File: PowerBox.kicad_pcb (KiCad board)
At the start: 2 copper layers, 71.1 x 76.2 mm, 7 parts, among them J1 Screw_Terminal_01x16, U1 MP1584EN, U2 MP1584EN, U3 MP1584EN, U4 MP1584EN, U5 MP1584EN, U6 MP1584EN

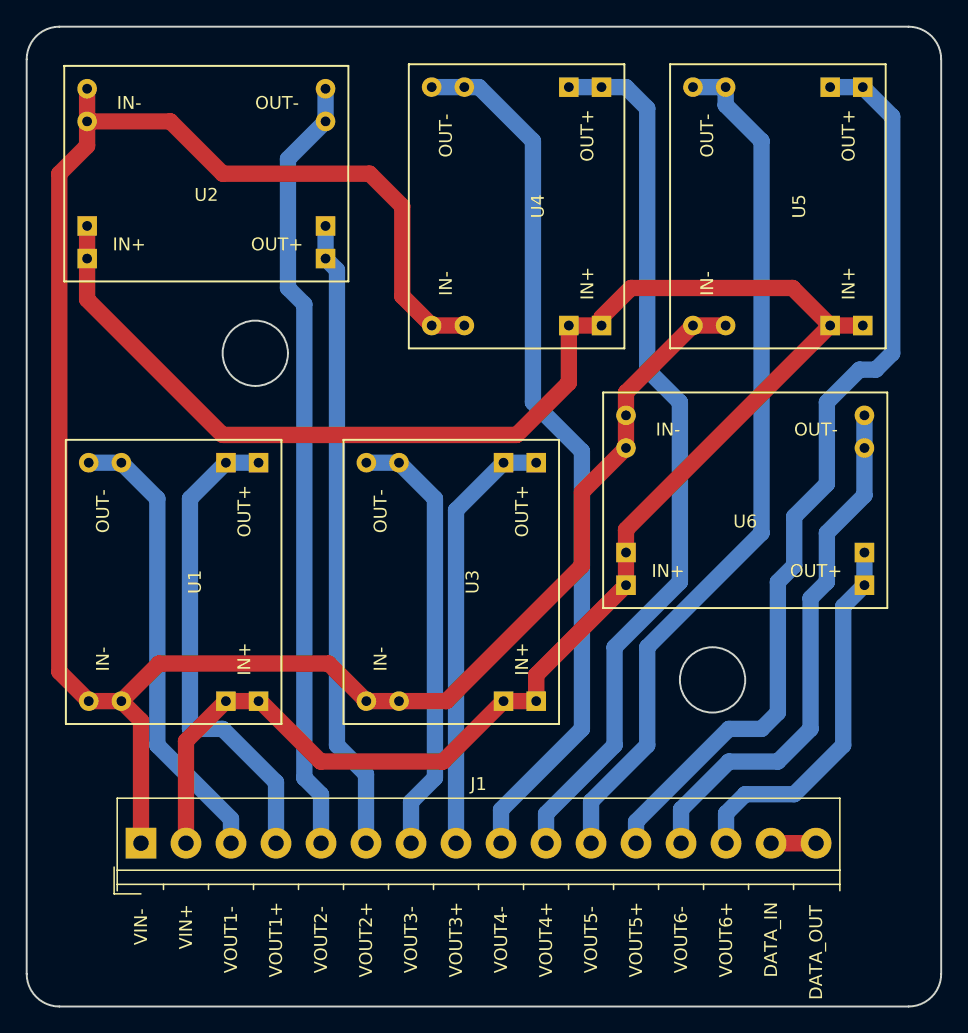
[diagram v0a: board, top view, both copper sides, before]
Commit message: rerouted some tracks away from screw holes, with 25 mil grid.
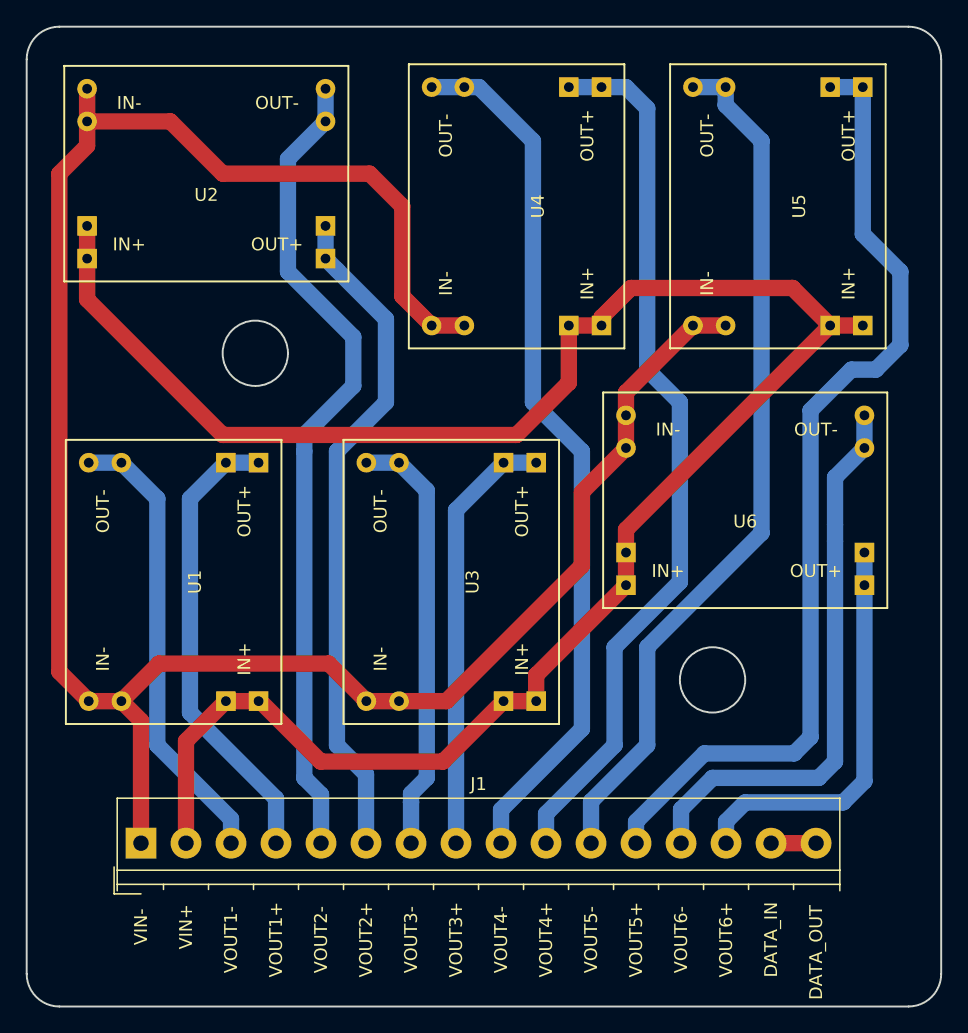
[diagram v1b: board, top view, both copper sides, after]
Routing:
- net Net-(J1-Pad12): track 72.8 -> 76.3 mm
- net Net-(J1-Pad5): track 60.9 -> 64.1 mm
- net Net-(J1-Pad6): track 49.3 -> 52.5 mm
- net Net-(J1-Pad13): track 41.4 -> 44.0 mm
- net Net-(J1-Pad14): track 29.3 -> 31.5 mm
- net Net-(J1-Pad4): track 38.0 -> 36.5 mm
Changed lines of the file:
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@@
     (thickness 1.6)
     (drawings 10)
-    (tracks 144)
+    (tracks 146)
     (zones 0)
     (modules 7)
@@
   (segment (start 111.76 106.68) (end 117.49 112.41) (width 1.27) (layer B.Cu) (net 3))
   (segment (start 117.49 112.41) (end 117.49 114.3) (width 1.27) (layer B.Cu) (net 3))
-  (segment (start 114.3 105.41) (end 116.84 105.41) (width 1.27) (layer B.Cu) (net 4))
-  (segment (start 114.3 87.503) (end 114.3 105.41) (width 1.27) (layer B.Cu) (net 4))
+  (segment (start 114.3 87.503) (end 114.3 104.14) (width 1.27) (layer B.Cu) (net 4))
   (segment (start 117.094 84.709) (end 114.3 87.503) (width 1.27) (layer B.Cu) (net 4))
-  (segment (start 120.99 109.56) (end 120.99 114.3) (width 1.27) (layer B.Cu) (net 4))
-  (segment (start 116.84 105.41) (end 120.99 109.56) (width 1.27) (layer B.Cu) (net 4))
+  (segment (start 120.99 110.83) (end 120.99 114.3) (width 1.27) (layer B.Cu) (net 4) (status 800000))
+  (segment (start 114.3 104.14) (end 120.99 110.83) (width 1.27) (layer B.Cu) (net 4))
   (segment (start 119.634 84.709) (end 117.094 84.709) (width 1.27) (layer B.Cu) (net 4))
   (segment (start 120.65 113.96) (end 120.99 114.3) (width 1.27) (layer B.Cu) (net 4))
-  (segment (start 124.841 55.626) (end 124.841 58.166) (width 1.27) (layer B.Cu) (net 5))
+  (segment (start 123.19 83.82) (end 123.19 82.55) (width 1.27) (layer B.Cu) (net 5))
   (segment (start 124.841 58.166) (end 121.92 61.087) (width 1.27) (layer B.Cu) (net 5))
-  (segment (start 121.92 61.087) (end 121.92 71.12) (width 1.27) (layer B.Cu) (net 5))
-  (segment (start 121.92 71.12) (end 123.19 72.39) (width 1.27) (layer B.Cu) (net 5))
-  (segment (start 123.19 72.39) (end 123.19 109.22) (width 1.27) (layer B.Cu) (net 5))
   (segment (start 123.19 109.22) (end 124.49 110.52) (width 1.27) (layer B.Cu) (net 5))
   (segment (start 124.49 110.52) (end 124.49 114.3) (width 1.27) (layer B.Cu) (net 5))
-  (segment (start 127.99 114.3) (end 127.99 108.94) (width 1.27) (layer B.Cu) (net 6))
-  (segment (start 125.73 69.723) (end 124.841 68.834) (width 1.27) (layer B.Cu) (net 6))
-  (segment (start 125.73 106.68) (end 125.73 69.723) (width 1.27) (layer B.Cu) (net 6))
+  (segment (start 123.19 109.22) (end 123.19 83.82) (width 1.27) (layer B.Cu) (net 5))
+  (segment (start 121.92 69.85) (end 121.92 61.087) (width 1.27) (layer B.Cu) (net 5))
+  (segment (start 127 74.93) (end 121.92 69.85) (width 1.27) (layer B.Cu) (net 5))
+  (segment (start 127 78.74) (end 127 74.93) (width 1.27) (layer B.Cu) (net 5))
+  (segment (start 123.19 82.55) (end 127 78.74) (width 1.27) (layer B.Cu) (net 5))
+  (segment (start 124.841 55.626) (end 124.841 58.166) (width 1.27) (layer B.Cu) (net 5))
+  (segment (start 125.73 106.68) (end 125.73 83.82) (width 1.27) (layer B.Cu) (net 6))
   (segment (start 127.99 108.94) (end 125.73 106.68) (width 1.27) (layer B.Cu) (net 6))
+  (segment (start 124.841 68.834) (end 125.73 69.723) (width 1.27) (layer B.Cu) (net 6))
+  (segment (start 127.99 108.94) (end 127.99 114.3) (width 1.27) (layer B.Cu) (net 6))
+  (segment (start 129.54 73.533) (end 125.73 69.723) (width 1.27) (layer B.Cu) (net 6))
+  (segment (start 129.54 80.01) (end 129.54 73.533) (width 1.27) (layer B.Cu) (net 6))
+  (segment (start 125.73 83.82) (end 129.54 80.01) (width 1.27) (layer B.Cu) (net 6))
   (segment (start 124.841 68.834) (end 124.841 66.294) (width 1.27) (layer B.Cu) (net 6))
+  (segment (start 131.49 111.125) (end 131.49 110.445) (width 1.27) (layer B.Cu) (net 7))
+  (segment (start 132.715 86.868) (end 130.556 84.709) (width 1.27) (layer B.Cu) (net 7) (status 800000))
+  (segment (start 132.715 109.22) (end 132.715 86.868) (width 1.27) (layer B.Cu) (net 7))
+  (segment (start 131.49 110.445) (end 132.715 109.22) (width 1.27) (layer B.Cu) (net 7))
   (segment (start 128.016 84.709) (end 130.556 84.709) (width 1.27) (layer B.Cu) (net 7))
-  (segment (start 130.556 84.709) (end 133.35 87.503) (width 1.27) (layer B.Cu) (net 7))
-  (segment (start 133.35 87.503) (end 133.35 109.22) (width 1.27) (layer B.Cu) (net 7))
-  (segment (start 133.35 109.22) (end 131.49 111.08) (width 1.27) (layer B.Cu) (net 7))
-  (segment (start 131.49 111.08) (end 131.49 114.3) (width 1.27) (layer B.Cu) (net 7))
+  (segment (start 131.49 111.08) (end 131.49 111.125) (width 1.27) (layer B.Cu) (net 7))
+  (segment (start 131.49 111.125) (end 131.49 114.3) (width 1.27) (layer B.Cu) (net 7))
   (segment (start 141.224 84.709) (end 138.684 84.709) (width 1.27) (layer B.Cu) (net 8))
   (segment (start 138.684 84.709) (end 134.99 88.403) (width 1.27) (layer B.Cu) (net 8))
@@
   (segment (start 155.956 55.499) (end 155.956 55.626) (width 1.27) (layer B.Cu) (net 11))
   (segment (start 153.416 55.499) (end 155.956 55.499) (width 1.27) (layer B.Cu) (net 11))
-  (segment (start 148.99 114.3) (end 148.99 112.63) (width 1.27) (layer B.Cu) (net 12))
-  (segment (start 168.91 57.785) (end 166.624 55.499) (width 1.27) (layer B.Cu) (net 12))
-  (segment (start 168.91 76.2) (end 168.91 57.785) (width 1.27) (layer B.Cu) (net 12))
-  (segment (start 167.64 77.47) (end 168.91 76.2) (width 1.27) (layer B.Cu) (net 12))
-  (segment (start 166.37 77.47) (end 167.64 77.47) (width 1.27) (layer B.Cu) (net 12))
-  (segment (start 163.83 80.01) (end 166.37 77.47) (width 1.27) (layer B.Cu) (net 12))
-  (segment (start 163.83 86.36) (end 163.83 80.01) (width 1.27) (layer B.Cu) (net 12))
-  (segment (start 161.29 88.9) (end 163.83 86.36) (width 1.27) (layer B.Cu) (net 12))
-  (segment (start 161.29 92.71) (end 161.29 88.9) (width 1.27) (layer B.Cu) (net 12))
-  (segment (start 160.02 93.98) (end 161.29 92.71) (width 1.27) (layer B.Cu) (net 12))
-  (segment (start 160.02 104.14) (end 160.02 93.98) (width 1.27) (layer B.Cu) (net 12))
-  (segment (start 158.75 105.41) (end 160.02 104.14) (width 1.27) (layer B.Cu) (net 12))
-  (segment (start 156.21 105.41) (end 158.75 105.41) (width 1.27) (layer B.Cu) (net 12))
-  (segment (start 148.99 112.63) (end 156.21 105.41) (width 1.27) (layer B.Cu) (net 12))
+  (segment (start 148.99 114.3) (end 148.99 112.63) (width 1.27) (layer B.Cu) (net 12) (status 400000))
+  (segment (start 166.624 66.929) (end 166.624 55.499) (width 1.27) (layer B.Cu) (net 12) (status 800000))
+  (segment (start 169.545 69.85) (end 166.624 66.929) (width 1.27) (layer B.Cu) (net 12))
+  (segment (start 169.545 75.565) (end 169.545 69.85) (width 1.27) (layer B.Cu) (net 12))
+  (segment (start 167.64 77.47) (end 169.545 75.565) (width 1.27) (layer B.Cu) (net 12))
+  (segment (start 165.735 77.47) (end 167.64 77.47) (width 1.27) (layer B.Cu) (net 12))
+  (segment (start 162.56 80.645) (end 165.735 77.47) (width 1.27) (layer B.Cu) (net 12))
+  (segment (start 162.56 106.045) (end 162.56 80.645) (width 1.27) (layer B.Cu) (net 12))
+  (segment (start 161.29 107.315) (end 162.56 106.045) (width 1.27) (layer B.Cu) (net 12))
+  (segment (start 154.305 107.315) (end 161.29 107.315) (width 1.27) (layer B.Cu) (net 12))
+  (segment (start 148.99 112.63) (end 154.305 107.315) (width 1.27) (layer B.Cu) (net 12))
   (segment (start 164.084 55.499) (end 166.624 55.499) (width 1.27) (layer B.Cu) (net 12))
-  (segment (start 166.751 83.566) (end 166.751 87.249) (width 1.27) (layer B.Cu) (net 13))
-  (segment (start 152.49 111.67) (end 152.49 114.3) (width 1.27) (layer B.Cu) (net 13))
-  (segment (start 156.21 107.95) (end 152.49 111.67) (width 1.27) (layer B.Cu) (net 13))
-  (segment (start 160.02 107.95) (end 156.21 107.95) (width 1.27) (layer B.Cu) (net 13))
-  (segment (start 162.56 105.41) (end 160.02 107.95) (width 1.27) (layer B.Cu) (net 13))
-  (segment (start 162.56 95.25) (end 162.56 105.41) (width 1.27) (layer B.Cu) (net 13))
-  (segment (start 163.83 93.98) (end 162.56 95.25) (width 1.27) (layer B.Cu) (net 13))
-  (segment (start 163.83 90.17) (end 163.83 93.98) (width 1.27) (layer B.Cu) (net 13))
-  (segment (start 166.751 87.249) (end 163.83 90.17) (width 1.27) (layer B.Cu) (net 13))
+  (segment (start 164.465 89.535) (end 164.465 85.852) (width 1.27) (layer B.Cu) (net 13))
+  (segment (start 154.94 109.22) (end 163.195 109.22) (width 1.27) (layer B.Cu) (net 13))
+  (segment (start 154.94 109.22) (end 152.49 111.67) (width 1.27) (layer B.Cu) (net 13))
+  (segment (start 152.49 114.3) (end 152.49 111.67) (width 1.27) (layer B.Cu) (net 13) (status 400000))
+  (segment (start 164.465 107.95) (end 164.465 90.805) (width 1.27) (layer B.Cu) (net 13))
+  (segment (start 163.195 109.22) (end 164.465 107.95) (width 1.27) (layer B.Cu) (net 13))
+  (segment (start 164.465 90.805) (end 164.465 89.535) (width 1.27) (layer B.Cu) (net 13))
+  (segment (start 164.465 85.852) (end 166.751 83.566) (width 1.27) (layer B.Cu) (net 13) (status 800000))
   (segment (start 166.751 81.026) (end 166.751 83.566) (width 1.27) (layer B.Cu) (net 13))
+  (segment (start 155.99 114.3) (end 155.99 112.615) (width 1.27) (layer B.Cu) (net 14) (status 400000))
+  (segment (start 166.751 109.474) (end 166.751 94.234) (width 1.27) (layer B.Cu) (net 14) (status 800000))
+  (segment (start 165.1 111.125) (end 166.751 109.474) (width 1.27) (layer B.Cu) (net 14))
+  (segment (start 157.48 111.125) (end 165.1 111.125) (width 1.27) (layer B.Cu) (net 14))
+  (segment (start 155.99 112.615) (end 157.48 111.125) (width 1.27) (layer B.Cu) (net 14))
   (segment (start 166.751 91.694) (end 166.751 94.234) (width 1.27) (layer B.Cu) (net 14))
-  (segment (start 166.751 94.234) (end 165.1 95.885) (width 1.27) (layer B.Cu) (net 14))
-  (segment (start 165.1 95.885) (end 165.1 106.68) (width 1.27) (layer B.Cu) (net 14))
-  (segment (start 165.1 106.68) (end 161.29 110.49) (width 1.27) (layer B.Cu) (net 14))
-  (segment (start 161.29 110.49) (end 157.48 110.49) (width 1.27) (layer B.Cu) (net 14))
-  (segment (start 157.48 110.49) (end 155.99 111.98) (width 1.27) (layer B.Cu) (net 14))
-  (segment (start 155.99 111.98) (end 155.99 114.3) (width 1.27) (layer B.Cu) (net 14))
   (segment (start 159.49 114.3) (end 162.99 114.3) (width 1.27) (layer F.Cu) (net 15))
 )
